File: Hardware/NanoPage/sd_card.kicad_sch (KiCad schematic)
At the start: 8 parts, among them J2 Micro_SD_Card_Det, U6 TPS22929D

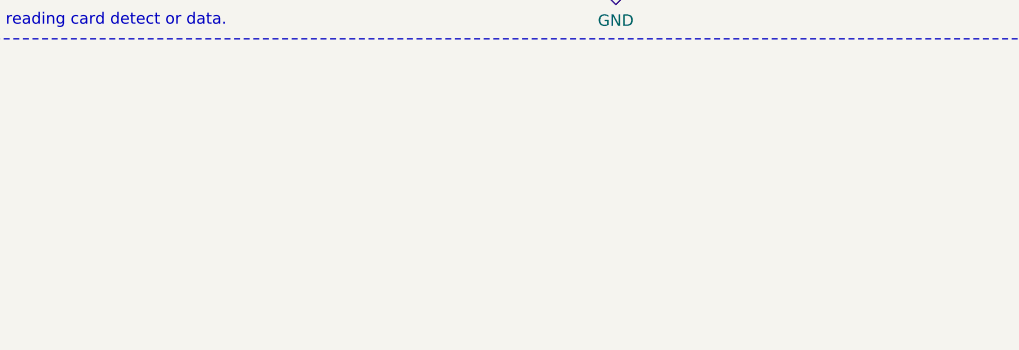
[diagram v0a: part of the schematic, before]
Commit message: docs: note to use separate SPI buses for SD card and EPD next design
Sharing one SPI bus between the two, gated only by a power switch on
the SD card, causes the EPD to misbehave whenever SD power is cut -
see the firmware-side writeup in .claude/CLAUDE.md for the full
root cause.
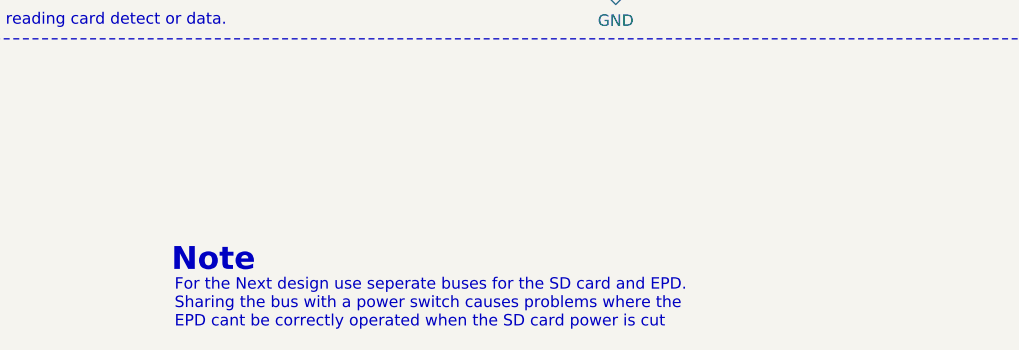
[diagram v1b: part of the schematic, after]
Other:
- note added: "For the Next design use seperate buses for the SD card and EPD. Sharing the bus with a power switch causes problems where the EPD cant be correctly operated when the SD card power is cut"
- note added: "Note"
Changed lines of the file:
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@@
+		)
+	)
+	(text "For the Next design use seperate buses for the SD card and EPD. \nSharing the bus with a power switch causes problems where the \nEPD cant be correctly operated when the SD card power is cut"
+		(exclude_from_sim no)
+		(at 109.728 190.754 0)
+		(effects
+			(font
+				(size 1.27 1.27)
+			)
+			(justify left)
 		)
 	)
@@
 				(bold yes)
 			)
+		)
+	)
+	(text "Note"
+		(exclude_from_sim no)
+		(at 114.046 185.928 0)
+		(effects
+			(font
+				(size 2.54 2.54)
+				(thickness 0.508)
+				(bold yes)
+			)
